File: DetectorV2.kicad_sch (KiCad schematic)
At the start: 22 parts, among them J1 Conn_01x02, U1 AD8092ARZ-REEL7

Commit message: updated
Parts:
- removed BT1: 9V, symbol Device:Battery_Cell
- added TP1: -, Connector_PinHeader_1.00mm:PinHeader_1x01_P1.00mm_Vertical, symbol Connector:TestPoint
- added TP2: +, Connector_PinHeader_1.00mm:PinHeader_1x01_P1.00mm_Vertical, symbol Connector:TestPoint
- U1: footprint (none) -> footprints:R_8_ADI
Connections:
- net GND: now also TP1.1; no longer C7.1
- net VCC: now also C7.1, TP2.1
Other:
- moved on the sheet: C7

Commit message: updated version - mit schalter + 47uF footprint
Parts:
- added SW2: SW_SPST, footprints:SSSS810701, symbol Switch:SW_SPST
- C7: footprint Capacitor_SMD:C_0805_2012Metric -> footprints:PCAP_EEHZ_D_PAN
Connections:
- net VCC: now also SW2.2 (B); no longer TP2.1
- new net: SW2.1 (A), TP2.1
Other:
- title: (none) -> Detector Version 2
- moved on the sheet: C1, C2, C3, C4, C5, C6, C7, D1, D2, D3, D4, J1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

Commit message: updated mit allen teilen aber fehlerhaft
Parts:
- added C2: 10p, Capacitor_SMD:C_0805_2012Metric, symbol Device:C
- C1: value 5p -> 10p
- renumbered C2 to C3, C3 to C4, C4 to C5, C5 to C6, C6 to C7, C7 to C8
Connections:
- net at C4.1, R3.2, U1.1 (OUT1): now also C2.2; no longer C1.2
- new net: C1.2, C2.1
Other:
- moved on the sheet: C1, C8, R3, SW2, TP2

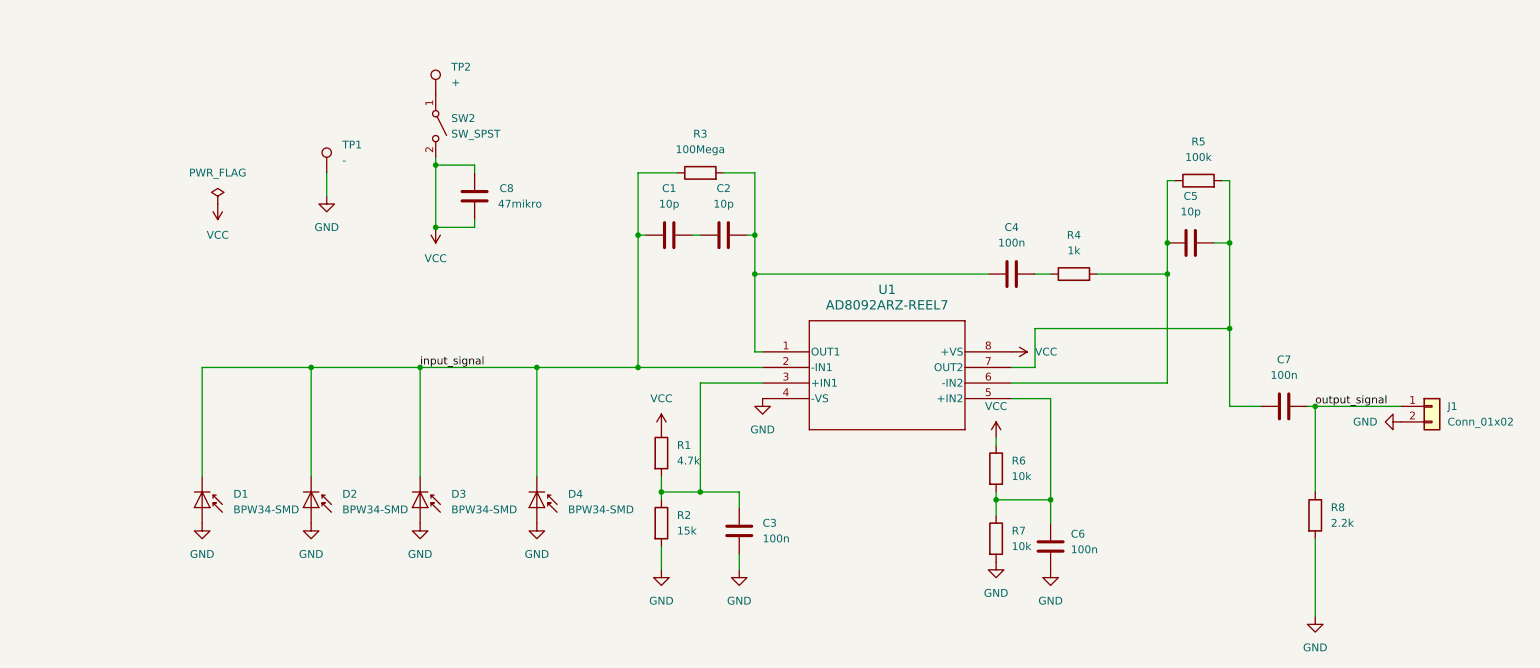
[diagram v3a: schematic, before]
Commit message: änderung von paar werten aus simulation
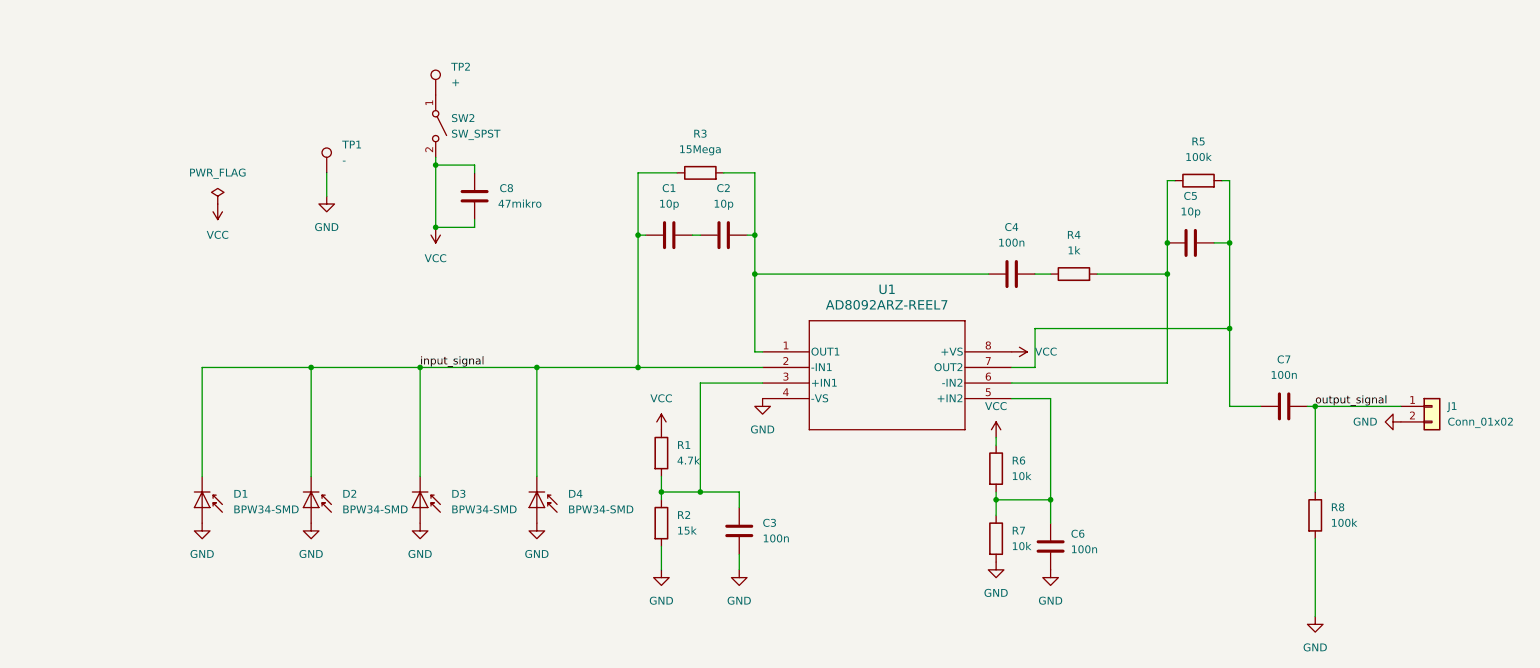
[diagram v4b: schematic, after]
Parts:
- R3: value 100Mega -> 15Mega
- R8: value 2.2k -> 100k
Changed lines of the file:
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@@
 			)
 		)
-		(property "Value" "100Mega"
+		(property "Value" "15Mega"
 			(at 127 64.77 90)
 			(effects
@@
 			)
 		)
-		(property "Value" "2.2k"
+		(property "Value" "100k"
 			(at 229.87 125.7299 0)
 			(effects
